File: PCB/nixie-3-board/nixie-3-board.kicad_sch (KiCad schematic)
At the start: 15 parts, among them Q1 MPSA92, Q4 MPSA42, U1 74141, U2 74141, U3 74HC595

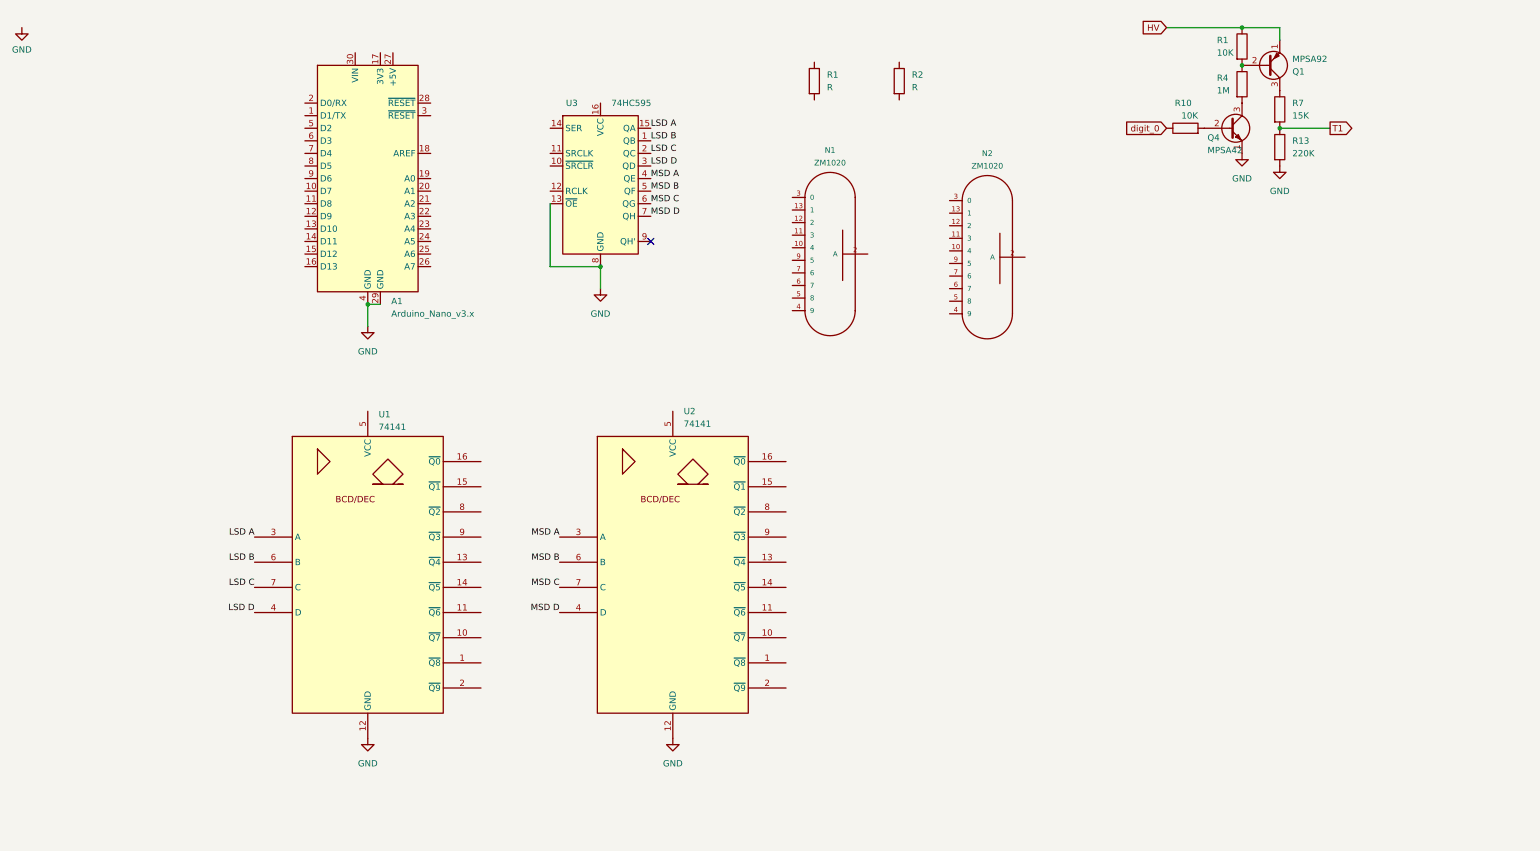
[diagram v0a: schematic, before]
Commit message: Updates: Added ShiftRegister74HC595, print.cc and modde_switch.cc
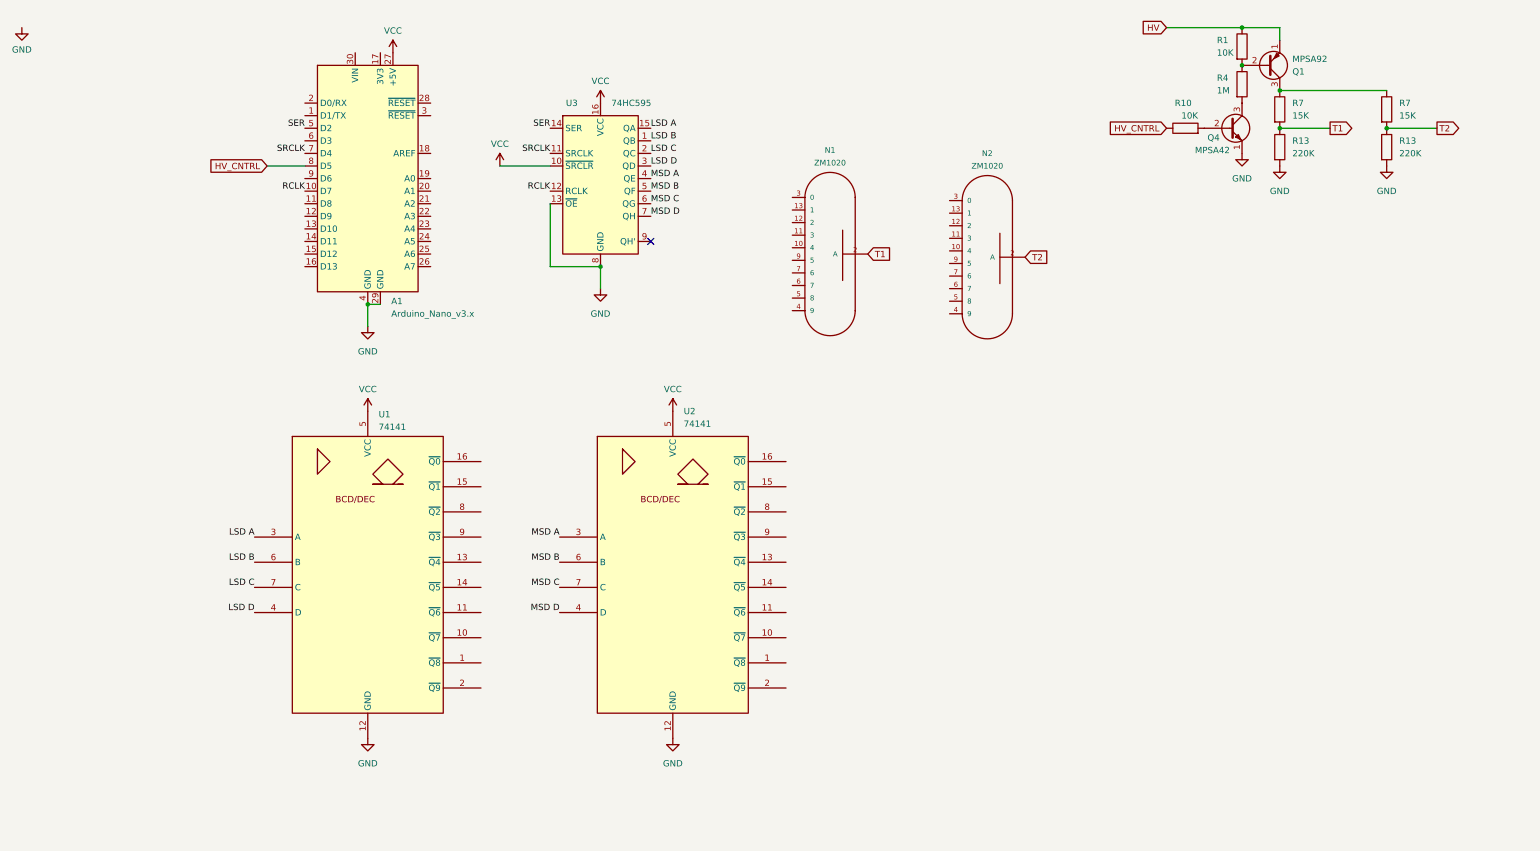
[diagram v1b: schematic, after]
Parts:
- removed R1, R2: R, symbol Device:R
- added R13: 220K, Resistor_THT:R_Axial_DIN0207_L6.3mm_D2.5mm_P7.62mm_Horizontal, symbol Device:R
- added R7: 15K, Resistor_THT:R_Axial_DIN0207_L6.3mm_D2.5mm_P7.62mm_Horizontal, symbol Device:R
- U1, U2, U3: footprint (none) -> Package_DIP:DIP-16_W7.62mm_Socket
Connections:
- net digit_0 is gone; now on net HV_CNTRL: R10.1
- net GND: now also R13.2
- net T1: now also N1.2 (A)
- net VCC: now reaches U3.10 (~{SRCLR})
- net VCC: now also A1.27 (+5V), U1.5 (VCC), U2.5 (VCC), U3.16 (VCC)
- net SRCLK: now reaches U3.11 (SRCLK)
- net SRCLK: now also A1.7 (D4)
- net RCLK: now reaches U3.12 (RCLK)
- net RCLK: now also A1.10 (D7)
- net SER: now reaches U3.14 (SER)
- net SER: now also A1.5 (D2)
- net T2: now reaches N2.2 (A)
- net T2: now also R13.1, R7.2
- net at Q1.3 (C), R7.1: now also R7.1
- net HV_CNTRL: now reaches A1.8 (D5)

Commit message: Added more stuff for PCB abd added docs
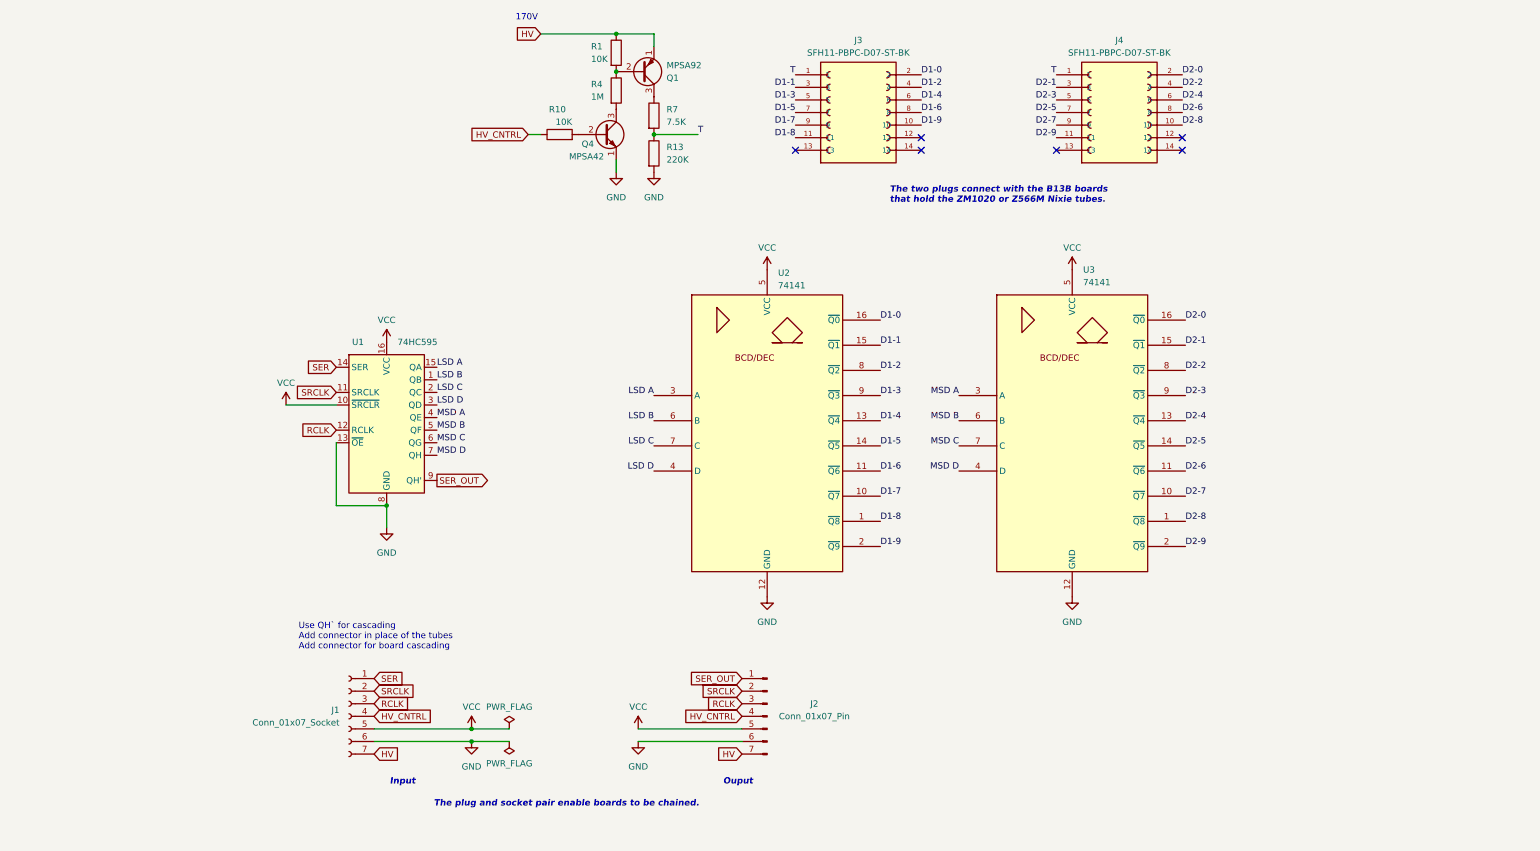
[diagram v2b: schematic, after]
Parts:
- removed A1: Arduino_Nano_v3.x, Module:Arduino_Nano, symbol nixie-3-symbols:Arduino_Nano_v3.x
- removed N1, N2: ZM1020, mynixies_6844A-D-SUB, symbol mynixies:ZM1020
- removed R13: 220K, Resistor_THT:R_Axial_DIN0207_L6.3mm_D2.5mm_P7.62mm_Horizontal, symbol Device:R
- removed R7: 15K, Resistor_THT:R_Axial_DIN0207_L6.3mm_D2.5mm_P7.62mm_Horizontal, symbol Device:R
- added J1: Conn_01x07_Socket, Connector_PinSocket_2.54mm:PinSocket_1x07_P2.54mm_Horizontal, symbol Connector:Conn_01x07_Socket
- added J2: Conn_01x07_Pin, Connector_PinHeader_2.54mm:PinHeader_1x07_P2.54mm_Horizontal, symbol Connector:Conn_01x07_Pin
- added J3, J4: SFH11-PBPC-D07-ST-BK, nixie-3-footprints:SULLINS_SFH11-PBPC-D07-ST-BK, symbol B13B-board-symbols:SFH11-PBPC-D07-ST-BK
- R7: value 15K -> 7.5K
- renumbered U3 to U1, U1 to U2, U2 to U3
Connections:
- net GND: now also J1.6 (Pin_6), J2.6 (Pin_6)
- net HV: now also J1.7 (Pin_7), J2.7 (Pin_7)
- net HV_CNTRL: now also J1.4 (Pin_4), J2.4 (Pin_4)
- net RCLK: now also J1.3 (Pin_3), J2.3 (Pin_3)
- net SER: now also J1.1 (Pin_1)
- net SRCLK: now also J1.2 (Pin_2), J2.2 (Pin_2)
- net VCC: now also J1.5 (Pin_5), J2.5 (Pin_5)
- net SER_OUT: now reaches U1.9 (QH')
- net SER_OUT: now also J2.1 (Pin_1)
- net D2-8: now reaches U3.1 (~{Q8})
- net D2-8: now also J4.10
- net D2-7: now reaches U3.10 (~{Q7})
- net D2-7: now also J4.9
- net D2-6: now reaches U3.11 (~{Q6})
- net D2-6: now also J4.8
- net D2-4: now reaches U3.13 (~{Q4})
- net D2-4: now also J4.6
- net D2-5: now reaches U3.14 (~{Q5})
- net D2-5: now also J4.7
- net D2-1: now reaches U3.15 (~{Q1})
- net D2-1: now also J4.3
- net D2-0: now reaches U3.16 (~{Q0})
- net D2-0: now also J4.2
- net D2-9: now reaches U3.2 (~{Q9})
- net D2-9: now also J4.11
- net D2-2: now reaches U3.8 (~{Q2})
- net D2-2: now also J4.4
- net D2-3: now reaches U3.9 (~{Q3})
- net D2-3: now also J4.5
- net D1-8: now reaches U2.1 (~{Q8})
- net D1-8: now also J3.11
- net D1-7: now reaches U2.10 (~{Q7})
- net D1-7: now also J3.9
- net D1-6: now reaches U2.11 (~{Q6})
- net D1-6: now also J3.8
- net D1-4: now reaches U2.13 (~{Q4})
- net D1-4: now also J3.6
- net D1-5: now reaches U2.14 (~{Q5})
- net D1-5: now also J3.7
- net D1-1: now reaches U2.15 (~{Q1})
- net D1-1: now also J3.3
- net D1-0: now reaches U2.16 (~{Q0})
- net D1-0: now also J3.2
- net D1-9: now reaches U2.2 (~{Q9})
- net D1-9: now also J3.10
- net D1-2: now reaches U2.8 (~{Q2})
- net D1-2: now also J3.4
- net D1-3: now reaches U2.9 (~{Q3})
- net D1-3: now also J3.5
- net T1 renamed T
- net T: now also J3.1, J4.1
- no-connect marks 1 -> 6
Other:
- note added: "170V"
- note added: "Input"
- note added: "Ouput"
- note added: "The plug and socket pair enable boards to be chained."
- note added: "The two plugs connect with the B13B boards that hold the ZM1020 or Z566M Nixie tubes."
- note added: "Use QH` for cascading Add connector in place of the tubes Add connector for board cascading"
- moved on the sheet: Q1, Q4, R1, R10, R13, R4, R7, U1, U2, U3

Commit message: new layout - might work. Needs holes, markings, screw terminals
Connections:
- net D1-8: now also J3.10; no longer J3.11
- net D1-9: now also J3.11; no longer J3.10
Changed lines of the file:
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@@
     (effects (font (size 1.27 1.27)) (justify right bottom))
   )
-  (label "D1-8" (at 142.24 46.99 180) (fields_autoplaced)
-    (effects (font (size 1.27 1.27)) (justify right bottom))
+  (label "D1-8" (at 167.64 44.45 0) (fields_autoplaced)
+    (effects (font (size 1.27 1.27)) (justify left bottom))
   )
   (label "D2-3" (at 220.98 99.06 0) (fields_autoplaced)
@@
     (effects (font (size 1.27 1.27)) (justify left bottom))
   )
-  (label "D1-9" (at 167.64 44.45 0) (fields_autoplaced)
-    (effects (font (size 1.27 1.27)) (justify left bottom))
+  (label "D1-9" (at 142.24 46.99 180) (fields_autoplaced)
+    (effects (font (size 1.27 1.27)) (justify right bottom))
   )
   (label "D2-8" (at 220.345 44.45 0) (fields_autoplaced)

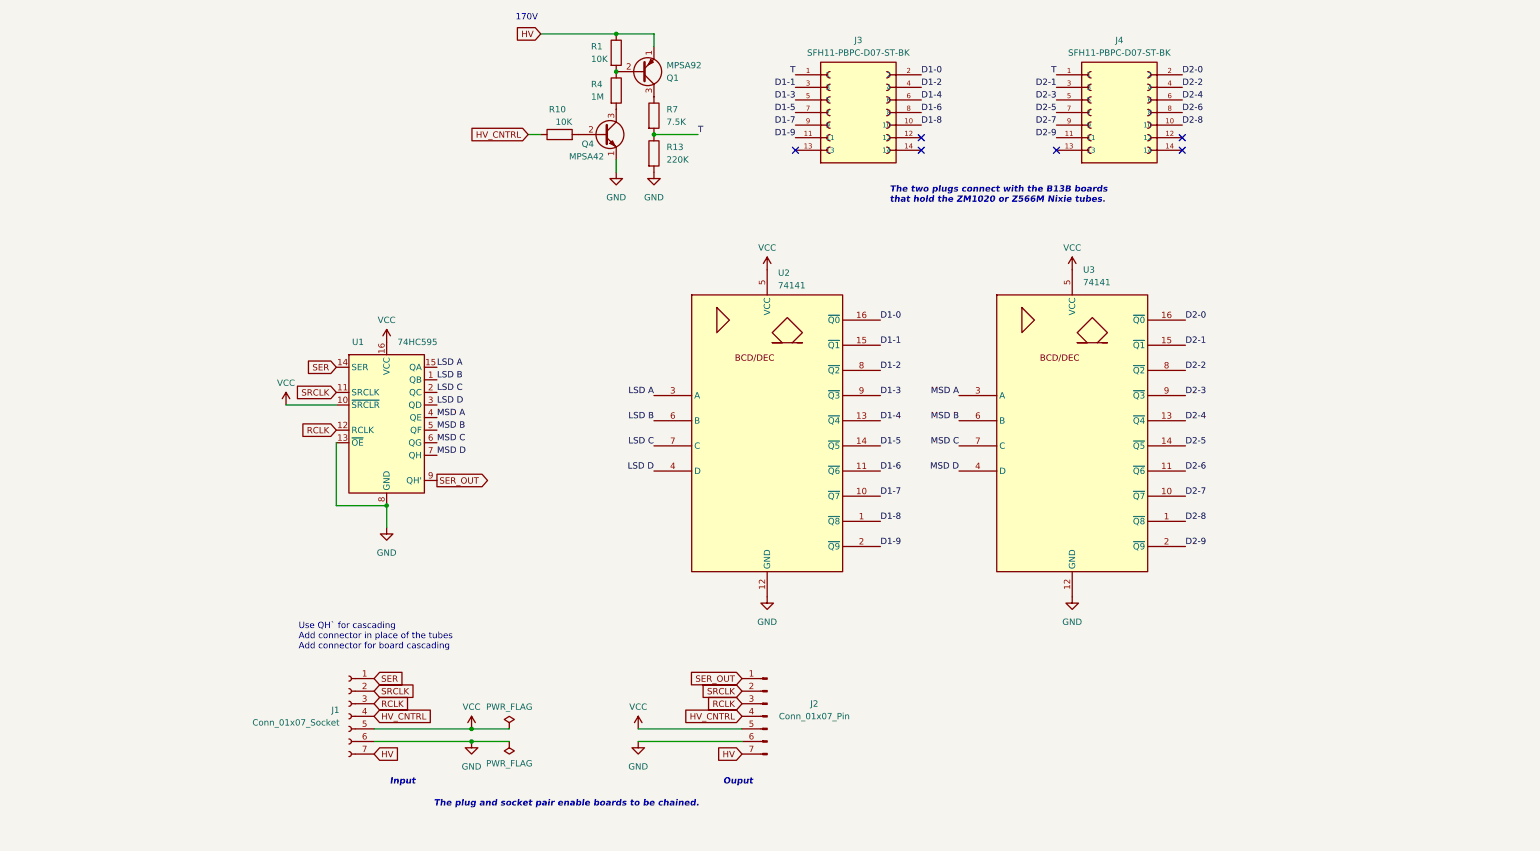
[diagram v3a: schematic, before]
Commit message: Version 3 of the driver PCB
Adds decouping caps and re-orders digits so LSD is on the right.
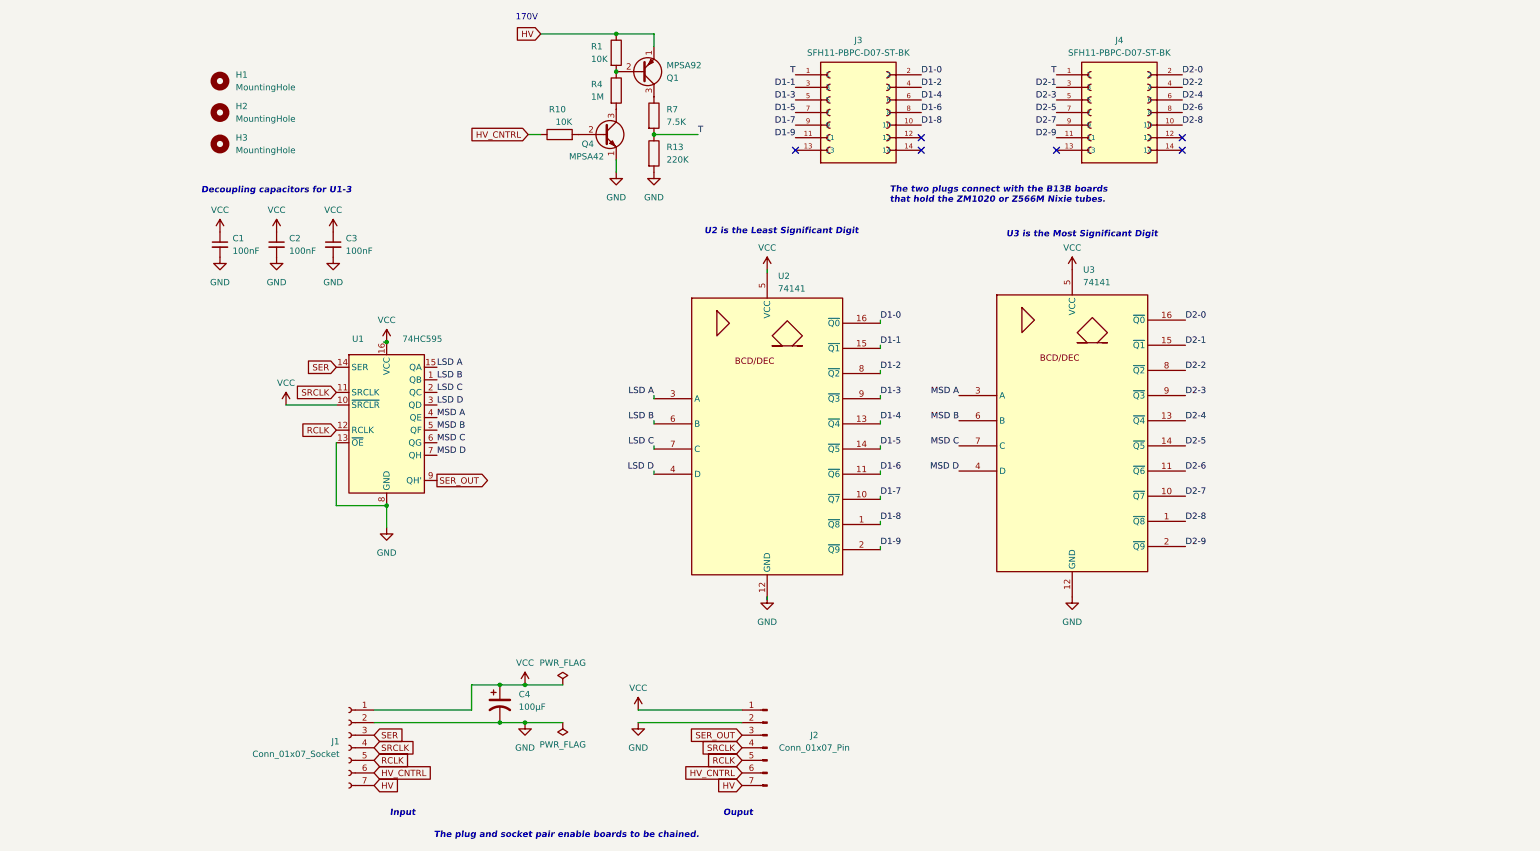
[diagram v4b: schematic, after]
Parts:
- added C1, C2, C3: 100nF, nixie-3-footprints:K104Z15Y5VF5TL2_VIS, symbol Device:C_Small
- added C4: 100µF, nixie-3-footprints:U1-E_NCH, symbol Device:C_Polarized_US
- added H1, H2, H3: MountingHole, MountingHole:MountingHole_2.7mm_M2.5_DIN965, symbol Mechanical:MountingHole
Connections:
- net GND: now also J1.2 (Pin_2), J2.2 (Pin_2), C1.2, C2.2, C3.2, C4.2; no longer J1.6 (Pin_6), J2.6 (Pin_6)
- net HV_CNTRL: now also J1.6 (Pin_6), J2.6 (Pin_6); no longer J1.4 (Pin_4), J2.4 (Pin_4)
- net RCLK: now also J1.5 (Pin_5), J2.5 (Pin_5); no longer J1.3 (Pin_3), J2.3 (Pin_3)
- net SER: now also J1.3 (Pin_3); no longer J1.1 (Pin_1)
- net SER_OUT: now also J2.3 (Pin_3); no longer J2.1 (Pin_1)
- net SRCLK: now also J1.4 (Pin_4), J2.4 (Pin_4); no longer J1.2 (Pin_2), J2.2 (Pin_2)
- net VCC: now also J1.1 (Pin_1), J2.1 (Pin_1), C1.1, C2.1, C3.1, C4.1; no longer J1.5 (Pin_5), J2.5 (Pin_5)
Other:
- note added: "Decoupling capacitors for U1-3"
- note added: "U2 is the Least Significant Digit"
- note added: "U3 is the Most Significant Digit"
- note removed: "Use QH` for cascading Add connector in place of the tubes Add connector for board cascading"
- company: (none) -> James Gallagher
- title: (none) -> Two Digit ZM1020 Driver Board
- moved on the sheet: J1, J2, U2
